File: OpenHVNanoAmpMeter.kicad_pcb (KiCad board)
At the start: 4 copper layers, 64.5 x 38 mm, 80 parts, among them J1 Conn_Coaxial, J2 Conn_Coaxial, J3 AVR-ISP-6, J4 Barrel_Jack_Switch, U1 DDC112U, U10 NCP1117-5.0_SOT223, U11 NCP1117-5.0_SOT223, U12 SN74LVC1G17DBVR, U13 SN74LVC1G17DBVR, U14 OPA340UA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

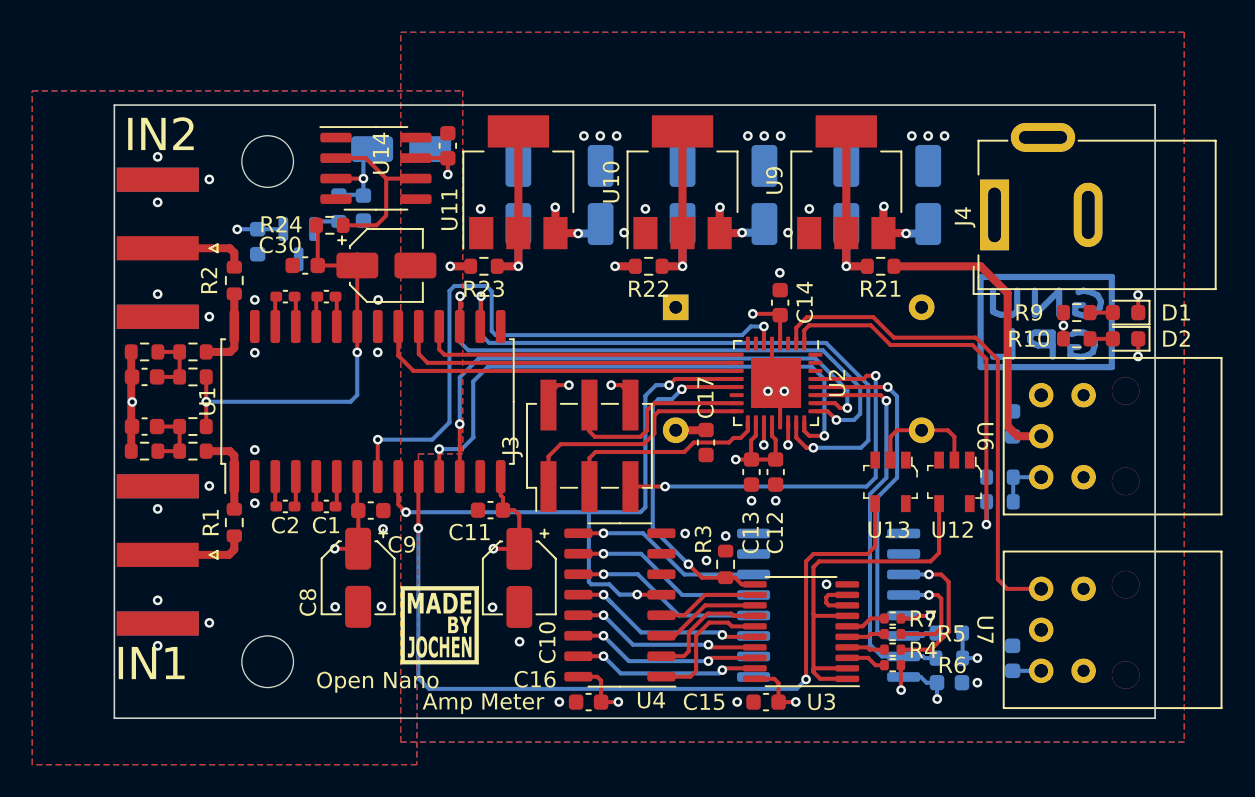
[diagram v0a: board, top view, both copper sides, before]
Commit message: DRC clean layout (incl. exclusion of violations)
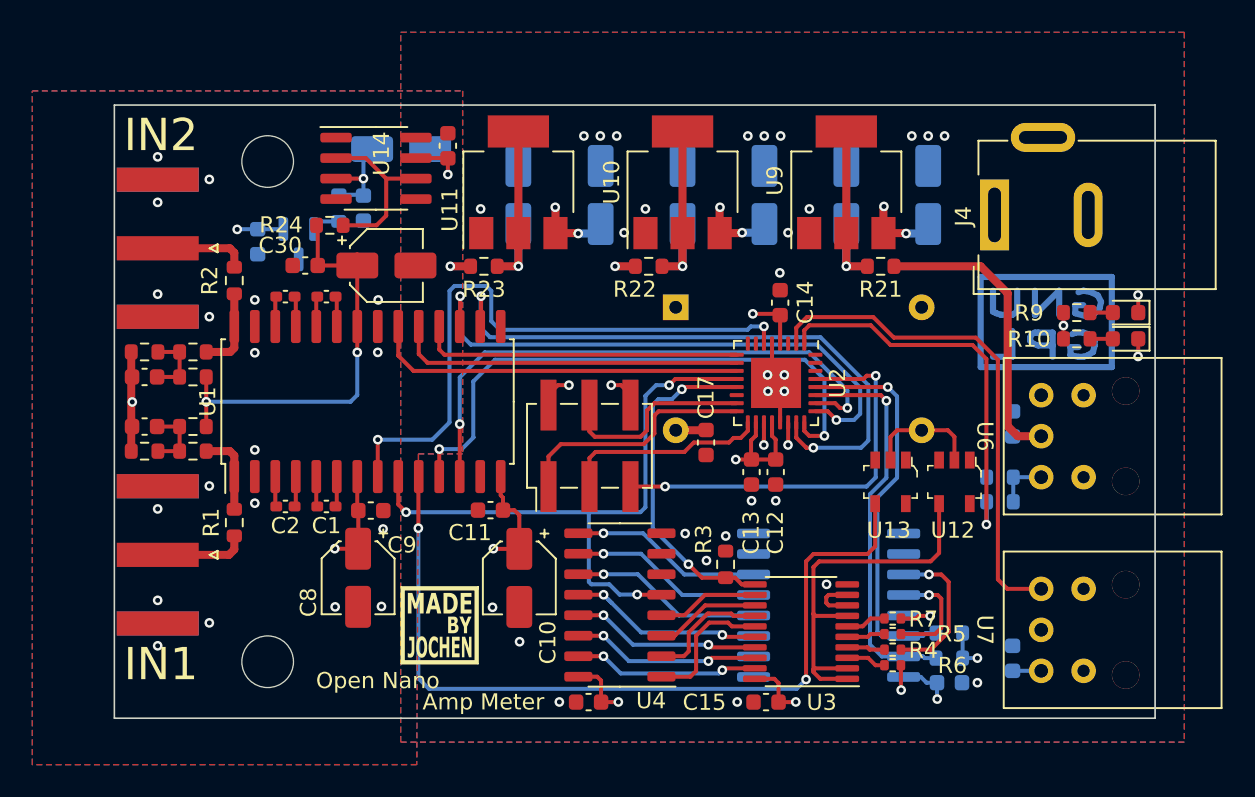
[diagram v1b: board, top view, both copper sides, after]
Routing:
- net /CurrentMeasurement/TEST: track 38.9 -> 38.3 mm
- net GND: track 5.85 -> 6.20 mm, vias 29 -> 31
